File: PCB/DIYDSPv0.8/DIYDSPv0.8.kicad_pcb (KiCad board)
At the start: 4 copper layers, 100 x 65 mm, 260 parts, among them J1 Conn_01x06, J10 Conn_01x05, J11 Conn_01x05, J12 Conn_01x05, J13 Conn_01x05, J2 Conn_01x05, J3 Conn_01x04, J4 Conn_01x04, J5 Conn_01x02, J6 Conn_01x05, J7 Conn_01x05, J8 Conn_01x05, J9 Conn_01x05, U1 ADAU1452, U4 AMS1117-1.2, X1 12.288MHz

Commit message: Updated v0.8 PCB for final version and added version for external ESP32 dev board.
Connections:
- R15 pad 1: +3V3 -> GND
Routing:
- net GND: vias 143 -> 144
- net +3V3: vias 15 -> 14
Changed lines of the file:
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@@
 			(layers "F.Cu" "F.Mask" "F.Paste")
 			(roundrect_rratio 0.25)
-			(net 1 "+3V3")
+			(net 2 "GND")
 			(pintype "passive")
 		)
@@
 	)
 	(via
-		(at 117.02 81.9)
-		(size 0.6)
-		(drill 0.3)
-		(layers "F.Cu" "B.Cu")
-		(net 1)
-	)
-	(via
 		(at 95.15 38.3915)
 		(size 0.6)
@@
 		(size 0.6)
 		(drill 0.3)
+		(layers "F.Cu" "B.Cu")
+		(net 2)
+	)
+	(via
+		(at 117.02 81.9)
+		(size 0.6)
+		(drill 0.3)

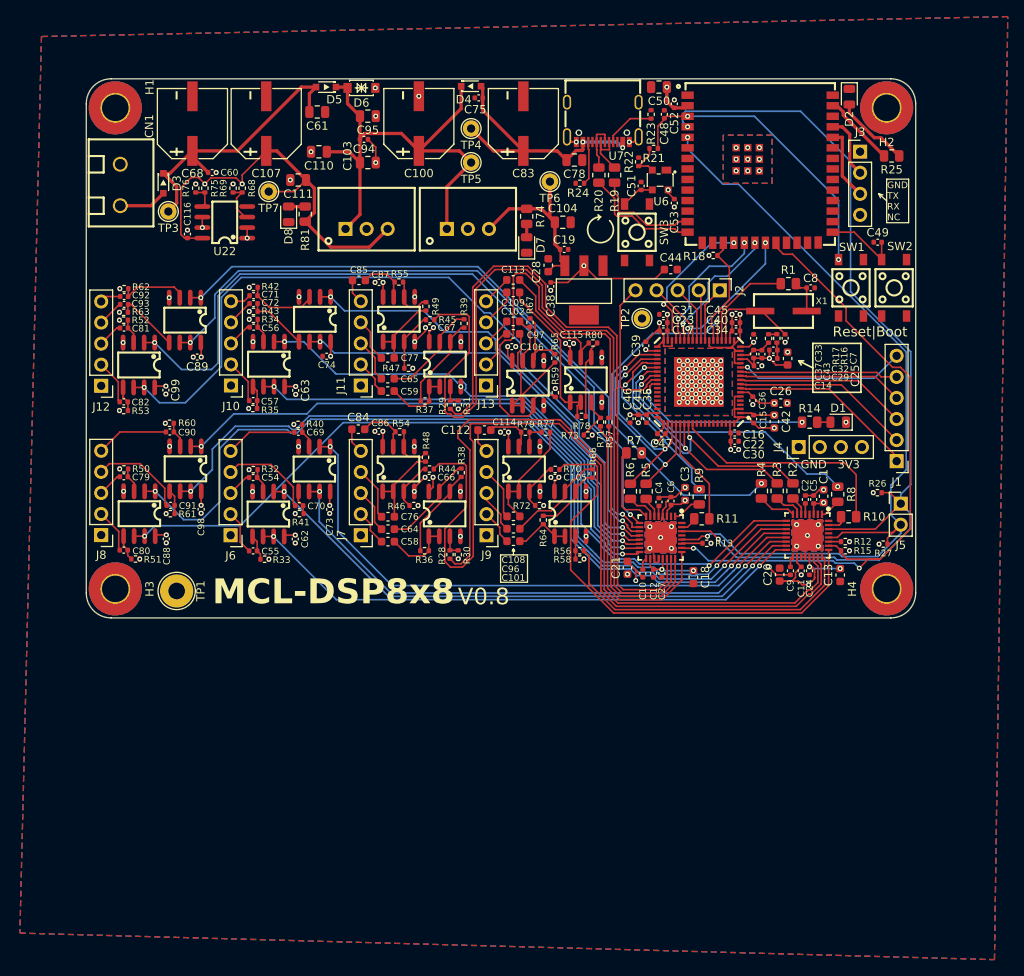
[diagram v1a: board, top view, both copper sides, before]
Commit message: Officially ordered v0.8 for validation - 12V input swapped for USB
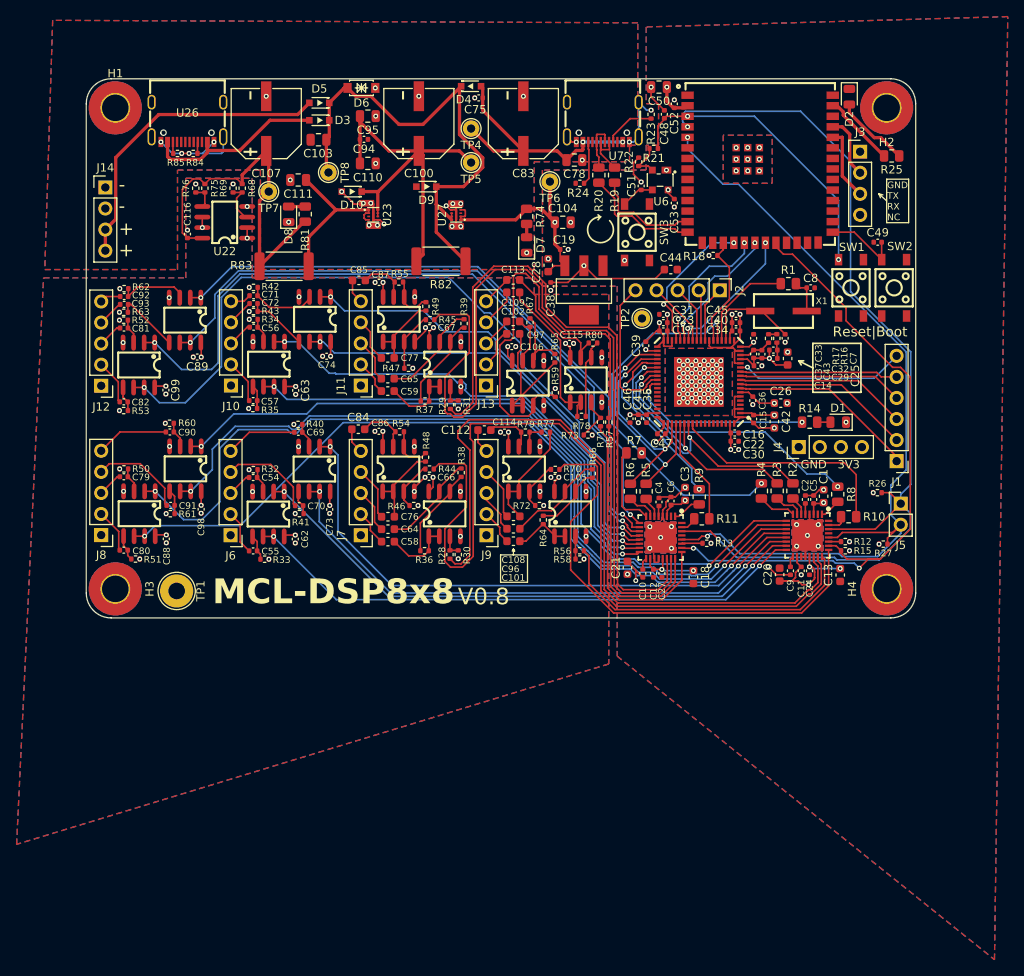
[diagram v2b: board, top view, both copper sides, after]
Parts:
- removed C60: 100n, Capacitor_SMD:C_0402_1005Metric
- removed C61: 22u, Capacitor_SMD:C_0805_2012Metric
- removed C68: 220uF, Custom:RVT1V221M0810
- removed CN1: ~, Custom:MX126-5.0-02P-GN01-Cu-S-A
- removed TP3: TestPoint, TestPoint:TestPoint_THTPad_D2.0mm_Drill1.0mm
- added D10: ~, Custom:DDZ5V6CSF-7, F.Cu at (57.0, 38.6)
- added D9: ~, Custom:DDZ5V6CSF-7, F.Cu at (66.0, 38.0)
- added J14: Conn_01x04, Connector_PinHeader_2.54mm:PinHeader_1x04_P2.54mm_Vertical, F.Cu at (27.3, 38.1)
- added R82: 0.2, Resistor_SMD:R_2512_6332Metric, F.Cu at (67.8, 47.0)
- added R83: 0.2, Resistor_SMD:R_2512_6332Metric, F.Cu at (48.9, 47.6)
- added R84: 5.1k, Resistor_SMD:R_0402_1005Metric, F.Cu at (37.9, 34.0)
- added R85: 5.1k, Resistor_SMD:R_0402_1005Metric, F.Cu at (36.0, 34.0)
- added TP8: TestPoint, TestPoint:TestPoint_THTPad_D2.0mm_Drill1.0mm, F.Cu at (54.2, 36.3)
- added U27: ~, Custom:SGM2039A-3.3XXEV8G_TR, F.Cu at (69.6, 41.4)
- C100, C107, C83: value 220uF -> 220u
- U23: footprint Custom:K7803-1000_C50396471 -> Custom:SGM2039A-3.3XXEV8G_TR
- U26: footprint Custom:K7803-1000_C50396471 -> Custom:GT-USB-7010ASV
- moved U26 25.1 mm to (37.2, 30.2), turned to 180 degrees
- moved D3 20.3 mm to (53.1, 30.0), turned to 180 degrees
- moved U23 11.5 mm to (59.6, 41.4), turned to -90 degrees
- moved C103 6.55 mm to (53.0, 32.4), turned to 0 degrees
- moved C110 6.06 mm to (59.0, 35.2), turned to 0 degrees
- moved D5 2.06 mm to (53.1, 27.9)
- turned H1 to 0 degrees
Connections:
- C100 pad 1: VCC -> VDD
- C110 pad 1: VCC -> VDD
- C111 pad 1: +3.3VA -> Net-(U23-FB)
- C94 pad 2: VCC -> VDD
- C95 pad 2: VCC -> VDD
- D3 pad 1: +12V -> VCC
- D3 pad 2: Net-(D3-A) -> VBUS2
- D5 pad 2: +12V -> VBUS3
- TP5 pad 1: VCC -> VDD
- U23 pad 1: VCC -> Net-(U23-FB)
- U23 pad 2: GND -> Net-(U23-FB)
- U23 pad 3: +3V3 -> unconnected-(U23-NC-Pad3)
- U26 pad 1: VCC -> GND
- U26 pad 3: +3.3VA -> GND
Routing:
- net GND: track 65.0 -> 170.7 mm, vias 144 -> 172
- net VDD: track 0.00 -> 47.6 mm
- net VBUS3: track 0.00 -> 37.8 mm
- net +12V: track 35.1 -> 0.00 mm
- net VBUS2: track 0.00 -> 22.4 mm
- net Net-(U23-FB): track 0.00 -> 19.3 mm
- net +3.3VA: track 103.8 -> 94.0 mm, vias 24 -> 22
- net Net-(D3-A): track 5.82 -> 0.00 mm
- net +1V2: track 83.4 -> 78.7 mm
- net +3V3: track 58.3 -> 62.5 mm, vias 14 -> 15
- net Net-(U19A-INA+): track 52.2 -> 50.8 mm
- net Net-(U26-CC2): track 0.00 -> 1.34 mm
- net Net-(U26-CC1): track 0.00 -> 1.34 mm
- net VBUS: track 32.2 -> 30.9 mm
- net VCC: track 58.7 -> 59.8 mm
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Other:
- board text added: "+ + - -"
- board text added: "5V DC"
- board text added: "USB Power Only 5V 1A"
- board text added: "USB Power+Program"
- board text removed: "+ -"
- board text removed: "12V DC"
